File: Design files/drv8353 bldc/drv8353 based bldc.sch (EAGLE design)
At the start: 119 parts, among them IC1 DRV8353RSRGZT, J3 2X6 FEMALE, J4 B06B-HCMKK

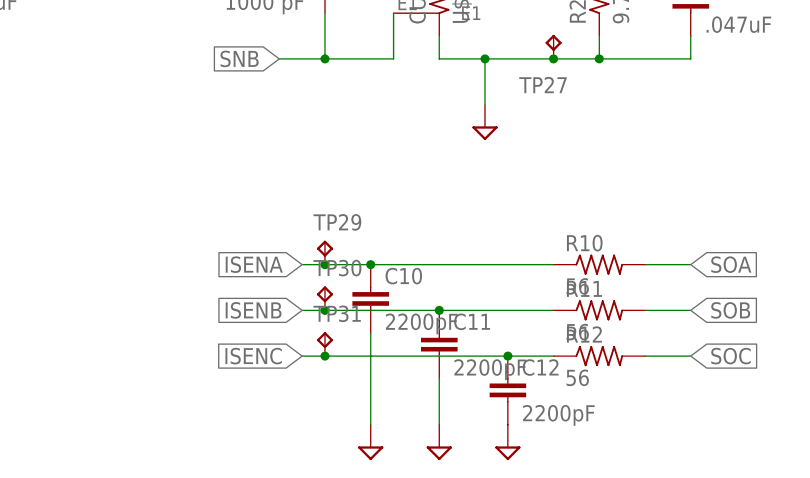
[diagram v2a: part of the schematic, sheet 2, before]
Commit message: remoeved extraneous test points
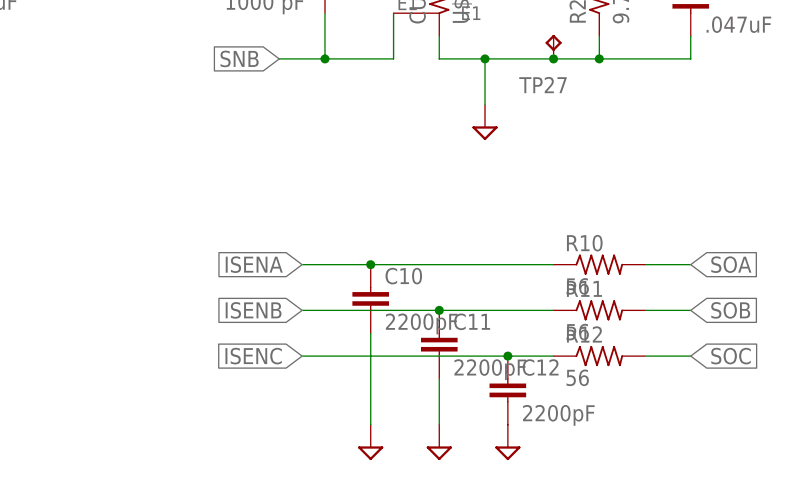
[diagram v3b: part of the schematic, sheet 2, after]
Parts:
- removed TP13, TP29, TP30, TP31, TP37, TP38, TP39: TPB1,27, testpad:TPB1,27
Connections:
- removed net N$17: TP39.TP, U$2.8
- removed net N$18: TP38.TP, U$2.6
- removed net N$19: TP37.TP, U$2.5
- net ISENA: no longer TP29.TP
- net ISENB: no longer TP30.TP
- net ISENC: no longer TP31.TP
- net VCP: no longer TP13.TP
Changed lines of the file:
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@@
 <?xml version="1.0" encoding="utf-8"?>
 <!DOCTYPE eagle SYSTEM "eagle.dtd">
-<eagle version="9.5.1">
+<eagle version="9.5.0">
 <drawing>
 <settings>
@@
 <part name="C21" library="rcl" library_urn="urn:adsk.eagle:library:334" deviceset="C-EU" device="C0805K" package3d_urn="urn:adsk.eagle:package:23681/2" value=".047 uF"/>
 <part name="C22" library="resistor" library_urn="urn:adsk.eagle:library:348" deviceset="C-EU" device="C0603K" package3d_urn="urn:adsk.eagle:package:26200/1" value="1 uF"/>
-<part name="TP13" library="testpad" library_urn="urn:adsk.eagle:library:385" deviceset="TP" device="B1,27" package3d_urn="urn:adsk.eagle:package:27944/2"/>
 <part name="C23" library="resistor" library_urn="urn:adsk.eagle:library:348" deviceset="C-EU" device="C0603K" package3d_urn="urn:adsk.eagle:package:26200/1" value=".1 uF"/>
 <part name="C25" library="rcl" library_urn="urn:adsk.eagle:library:334" deviceset="C-EU" device="C0805K" package3d_urn="urn:adsk.eagle:package:23681/2" value=".1 uF"/>
@@
 <part name="TP11" library="testpad" library_urn="urn:adsk.eagle:library:385" deviceset="TP" device="B1,27" package3d_urn="urn:adsk.eagle:package:27944/2"/>
 <part name="TP12" library="testpad" library_urn="urn:adsk.eagle:library:385" deviceset="TP" device="B1,27" package3d_urn="urn:adsk.eagle:package:27944/2"/>
-<part name="TP29" library="testpad" library_urn="urn:adsk.eagle:library:385" deviceset="TP" device="B1,27" package3d_urn="urn:adsk.eagle:package:27944/2"/>
-<part name="TP30" library="testpad" library_urn="urn:adsk.eagle:library:385" deviceset="TP" device="B1,27" package3d_urn="urn:adsk.eagle:package:27944/2"/>
-<part name="TP31" library="testpad" library_urn="urn:adsk.eagle:library:385" deviceset="TP" device="B1,27" package3d_urn="urn:adsk.eagle:package:27944/2"/>
 <part name="TP32" library="testpad" library_urn="urn:adsk.eagle:library:385" deviceset="TP" device="B1,27" package3d_urn="urn:adsk.eagle:package:27944/2"/>
 <part name="TP33" library="testpad" library_urn="urn:adsk.eagle:library:385" deviceset="TP" device="B1,27" package3d_urn="urn:adsk.eagle:package:27944/2"/>
@@
 <part name="TP35" library="testpad" library_urn="urn:adsk.eagle:library:385" deviceset="TP" device="B1,27" package3d_urn="urn:adsk.eagle:package:27944/2"/>
 <part name="TP36" library="testpad" library_urn="urn:adsk.eagle:library:385" deviceset="TP" device="B1,27" package3d_urn="urn:adsk.eagle:package:27944/2"/>
-<part name="TP37" library="testpad" library_urn="urn:adsk.eagle:library:385" deviceset="TP" device="B1,27" package3d_urn="urn:adsk.eagle:package:27944/2"/>
-<part name="TP38" library="testpad" library_urn="urn:adsk.eagle:library:385" deviceset="TP" device="B1,27" package3d_urn="urn:adsk.eagle:package:27944/2"/>
-<part name="TP39" library="testpad" library_urn="urn:adsk.eagle:library:385" deviceset="TP" device="B1,27" package3d_urn="urn:adsk.eagle:package:27944/2"/>
 <part name="U$16" library="REV BLDC" deviceset="SB50" device=""/>
 <part name="R18" library="rcl" library_urn="urn:adsk.eagle:library:334" deviceset="R-US_" device="R0603" package3d_urn="urn:adsk.eagle:package:23555/3" value="383k"/>
@@
 <attribute name="VALUE" x="-20.701" y="-54.356" size="1.778" layer="96" rot="R90"/>
 </instance>
-<instance part="TP13" gate="G$1" x="-17.78" y="-58.42" smashed="yes" rot="R180">
-<attribute name="NAME" x="-16.51" y="-59.69" size="1.778" layer="95" rot="R180"/>
-<attribute name="TP_SIGNAL_NAME" x="-19.05" y="-57.15" size="1.778" layer="97" rot="R180"/>
-</instance>
 <instance part="C23" gate="G$1" x="60.96" y="-68.58" smashed="yes">
 <attribute name="NAME" x="62.484" y="-68.199" size="1.778" layer="95"/>
@@
 <attribute name="NAME" x="-3.81" y="-62.23" size="1.778" layer="95" rot="R180"/>
 <attribute name="TP_SIGNAL_NAME" x="-3.81" y="-59.69" size="1.778" layer="97" rot="R180"/>
-</instance>
-<instance part="TP37" gate="G$1" x="-76.2" y="-127" smashed="yes" rot="R90">
-<attribute name="TP_SIGNAL_NAME" x="-74.93" y="-125.73" size="1.778" layer="97" rot="R90"/>
-</instance>
-<instance part="TP38" gate="G$1" x="-76.2" y="-129.54" smashed="yes" rot="R90">
-<attribute name="TP_SIGNAL_NAME" x="-74.93" y="-128.27" size="1.778" layer="97" rot="R90"/>
-</instance>
-<instance part="TP39" gate="G$1" x="-76.2" y="-134.62" smashed="yes" rot="R90">
-<attribute name="TP_SIGNAL_NAME" x="-74.93" y="-133.35" size="1.778" layer="97" rot="R90"/>
 </instance>
 <instance part="BB2" gate="1" x="119.38" y="-104.14" smashed="yes">
@@
 <segment>
 <pinref part="IC1" gate="G$1" pin="VCP"/>
-<wire x1="-2.54" y1="-55.88" x2="-17.78" y2="-55.88" width="0.1524" layer="91"/>
+<wire x1="-2.54" y1="-55.88" x2="-20.32" y2="-55.88" width="0.1524" layer="91"/>
 <pinref part="C22" gate="G$1" pin="2"/>
-<pinref part="TP13" gate="G$1" pin="TP"/>
-<wire x1="-17.78" y1="-55.88" x2="-20.32" y2="-55.88" width="0.1524" layer="91"/>
-<junction x="-17.78" y="-55.88"/>
 </segment>
 </net>
@@
 <pinref part="R4" gate="G$1" pin="1"/>
 <wire x1="-68.58" y1="-83.82" x2="-55.88" y2="-83.82" width="0.1524" layer="91"/>
-</segment>
-</net>
-<net name="N$17" class="0">
-<segment>
-<wire x1="-68.58" y1="-134.62" x2="-73.66" y2="-134.62" width="0.1524" layer="91"/>
-<pinref part="TP39" gate="G$1" pin="TP"/>
-<pinref part="U$2" gate="G$1" pin="8"/>
-</segment>
-</net>
-<net name="N$18" class="0">
-<segment>
-<wire x1="-68.58" y1="-129.54" x2="-73.66" y2="-129.54" width="0.1524" layer="91"/>
-<pinref part="TP38" gate="G$1" pin="TP"/>
-<pinref part="U$2" gate="G$1" pin="6"/>
-</segment>
-</net>
-<net name="N$19" class="0">
-<segment>
-<wire x1="-68.58" y1="-127" x2="-73.66" y2="-127" width="0.1524" layer="91"/>
-<pinref part="TP37" gate="G$1" pin="TP"/>
-<pinref part="U$2" gate="G$1" pin="5"/>
 </segment>
 </net>
@@
 <attribute name="NAME" x="114.935" y="58.674" size="1.778" layer="95" rot="R90"/>
 <attribute name="VALUE" x="120.269" y="58.674" size="1.778" layer="96" rot="R90"/>
-</instance>
-<instance part="TP29" gate="G$1" x="15.24" y="-15.24" smashed="yes">
-<attribute name="NAME" x="13.97" y="-13.97" size="1.778" layer="95"/>
-<attribute name="TP_SIGNAL_NAME" x="16.51" y="-16.51" size="1.778" layer="97"/>
-</instance>
-<instance part="TP30" gate="G$1" x="15.24" y="-20.32" smashed="yes">
-<attribute name="NAME" x="13.97" y="-19.05" size="1.778" layer="95"/>
-<attribute name="TP_SIGNAL_NAME" x="16.51" y="-21.59" size="1.778" layer="97"/>
-</instance>
-<instance part="TP31" gate="G$1" x="15.24" y="-25.4" smashed="yes">
-<attribute name="NAME" x="13.97" y="-24.13" size="1.778" layer="95"/>
-<attribute name="TP_SIGNAL_NAME" x="16.51" y="-26.67" size="1.778" layer="97"/>
 </instance>
 <instance part="U$3" gate="G$1" x="-55.88" y="12.7" smashed="yes" rot="MR90">
@@
 <wire x1="40.64" y1="-17.78" x2="20.32" y2="-17.78" width="0.1524" layer="91"/>
 <pinref part="C10" gate="G$1" pin="1"/>
-<wire x1="20.32" y1="-17.78" x2="15.24" y2="-17.78" width="0.1524" layer="91"/>
+<wire x1="20.32" y1="-17.78" x2="12.7" y2="-17.78" width="0.1524" layer="91"/>
 <junction x="20.32" y="-17.78"/>
 <label x="12.7" y="-17.78" size="1.778" layer="95" rot="R180" xref="yes"/>
-<pinref part="TP29" gate="G$1" pin="TP"/>
-<wire x1="15.24" y1="-17.78" x2="12.7" y2="-17.78" width="0.1524" layer="91"/>
-<junction x="15.24" y="-17.78"/>
 </segment>
 </net>
@@
 <wire x1="40.64" y1="-22.86" x2="27.94" y2="-22.86" width="0.1524" layer="91"/>
 <pinref part="C11" gate="G$1" pin="1"/>
-<wire x1="27.94" y1="-22.86" x2="15.24" y2="-22.86" width="0.1524" layer="91"/>
+<wire x1="27.94" y1="-22.86" x2="12.7" y2="-22.86" width="0.1524" layer="91"/>
 <junction x="27.94" y="-22.86"/>
 <label x="12.7" y="-22.86" size="1.778" layer="95" rot="R180" xref="yes"/>
-<pinref part="TP30" gate="G$1" pin="TP"/>
-<wire x1="15.24" y1="-22.86" x2="12.7" y2="-22.86" width="0.1524" layer="91"/>
-<junction x="15.24" y="-22.86"/>
 </segment>
 </net>
@@
 <wire x1="40.64" y1="-27.94" x2="35.56" y2="-27.94" width="0.1524" layer="91"/>
 <pinref part="C12" gate="G$1" pin="1"/>
-<wire x1="35.56" y1="-27.94" x2="15.24" y2="-27.94" width="0.1524" layer="91"/>
+<wire x1="35.56" y1="-27.94" x2="12.7" y2="-27.94" width="0.1524" layer="91"/>
 <junction x="35.56" y="-27.94"/>
 <label x="12.7" y="-27.94" size="1.778" layer="95" rot="R180" xref="yes"/>
-<pinref part="TP31" gate="G$1" pin="TP"/>
-<wire x1="15.24" y1="-27.94" x2="12.7" y2="-27.94" width="0.1524" layer="91"/>
-<junction x="15.24" y="-27.94"/>
-</segment>
-</net>
+</segment>
+</net>

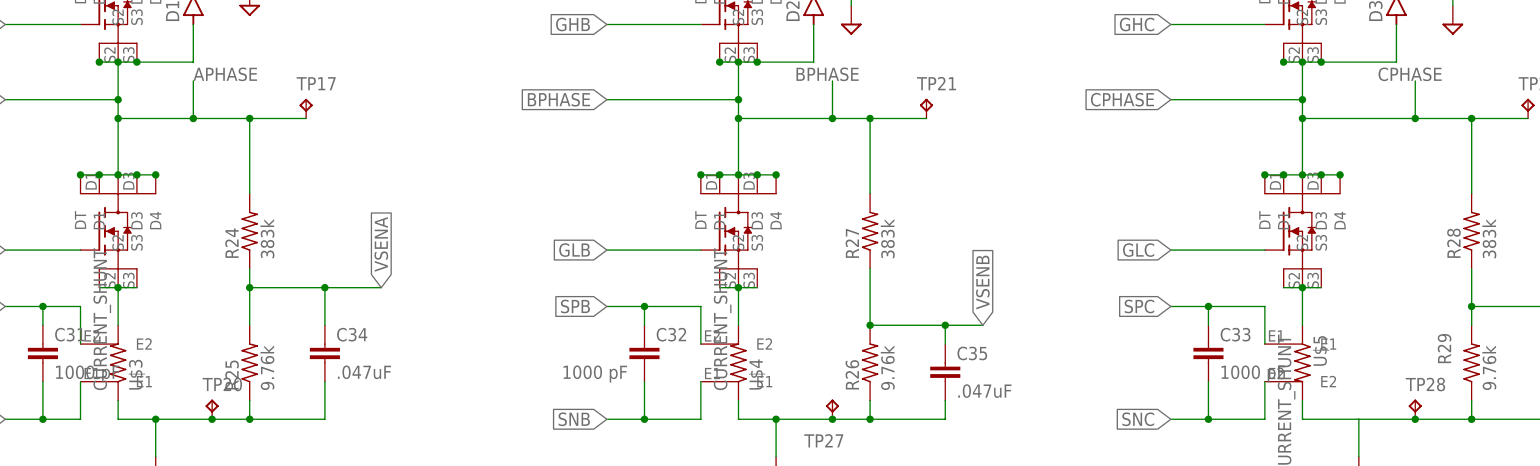
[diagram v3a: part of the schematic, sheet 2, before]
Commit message: added low side flybacks
added low side flybacks
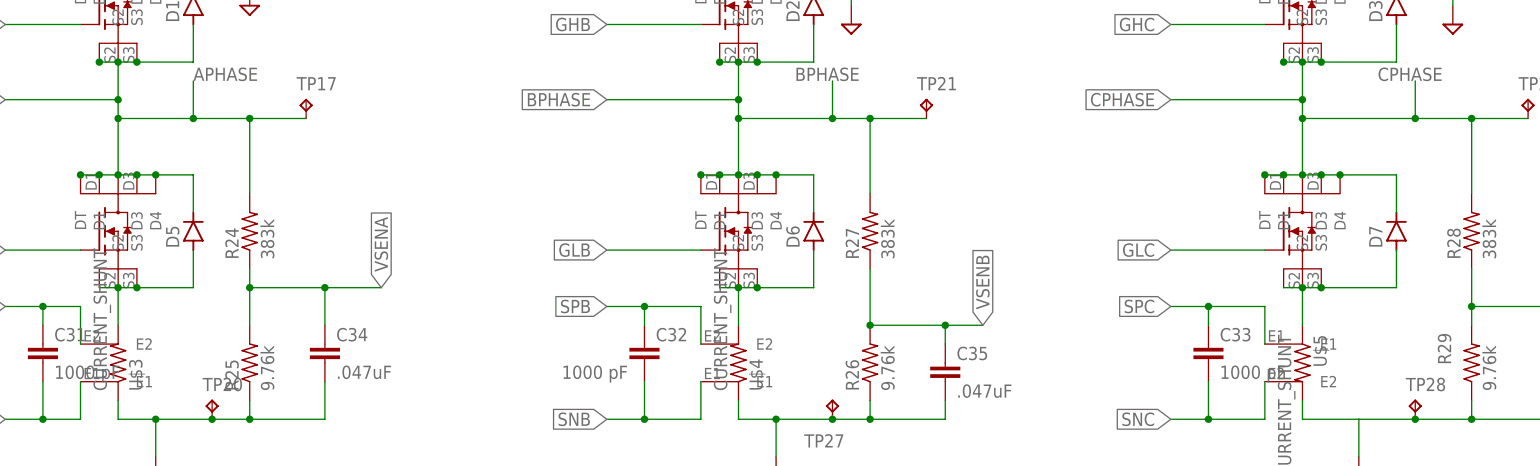
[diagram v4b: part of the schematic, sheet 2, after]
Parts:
- added D5, D6, D7: (no value), REV BLDC:D-SOD123
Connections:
- net APHASE: now also D5.C
- net BPHASE: now also D6.C
- net CPHASE: now also D7.C
- net N$22: now also D6.A
- net N$24: now also D5.A
- net N$27: now also D7.A
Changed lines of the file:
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@@
 <part name="R5" library="resistor" library_urn="urn:adsk.eagle:library:348" deviceset="R-US_" device="R0603" package3d_urn="urn:adsk.eagle:package:26057/1" value="0"/>
 <part name="TP19" library="testpad" library_urn="urn:adsk.eagle:library:385" deviceset="TP" device="B1,27" package3d_urn="urn:adsk.eagle:package:27944/2"/>
+<part name="D5" library="REV BLDC" deviceset="D-" device="SOD123" package3d_urn="urn:adsk.eagle:package:26308/2"/>
+<part name="D6" library="REV BLDC" deviceset="D-" device="SOD123" package3d_urn="urn:adsk.eagle:package:26308/2"/>
+<part name="D7" library="REV BLDC" deviceset="D-" device="SOD123" package3d_urn="urn:adsk.eagle:package:26308/2"/>
 </parts>
 <sheets>
@@
 <attribute name="NAME" x="125.984" y="71.501" size="1.778" layer="95"/>
 <attribute name="VALUE" x="125.984" y="66.421" size="1.778" layer="96"/>
+</instance>
+<instance part="D5" gate="G$1" x="-45.72" y="30.48" smashed="yes" rot="R90">
+<attribute name="NAME" x="-47.625" y="28.194" size="1.778" layer="95" rot="R90"/>
+<attribute name="VALUE" x="-41.021" y="27.686" size="1.778" layer="96" rot="R90"/>
+</instance>
+<instance part="D6" gate="G$1" x="38.1" y="30.48" smashed="yes" rot="R90">
+<attribute name="NAME" x="36.195" y="28.194" size="1.778" layer="95" rot="R90"/>
+<attribute name="VALUE" x="42.799" y="27.686" size="1.778" layer="96" rot="R90"/>
+</instance>
+<instance part="D7" gate="G$1" x="116.84" y="30.48" smashed="yes" rot="R90">
+<attribute name="NAME" x="114.935" y="28.194" size="1.778" layer="95" rot="R90"/>
+<attribute name="VALUE" x="121.539" y="27.686" size="1.778" layer="96" rot="R90"/>
 </instance>
 </instances>
@@
 <pinref part="U$3" gate="G$1" pin="I2"/>
 <wire x1="-55.88" y1="17.78" x2="-55.88" y2="22.86" width="0.1524" layer="91"/>
+<pinref part="D5" gate="G$1" pin="A"/>
+<wire x1="-45.72" y1="27.94" x2="-45.72" y2="22.86" width="0.1524" layer="91"/>
+<wire x1="-45.72" y1="22.86" x2="-53.34" y2="22.86" width="0.1524" layer="91"/>
+<junction x="-53.34" y="22.86"/>
 </segment>
 </net>
@@
 <pinref part="U$4" gate="G$1" pin="I2"/>
 <wire x1="27.94" y1="17.78" x2="27.94" y2="22.86" width="0.1524" layer="91"/>
+<pinref part="D6" gate="G$1" pin="A"/>
+<wire x1="38.1" y1="27.94" x2="38.1" y2="22.86" width="0.1524" layer="91"/>
+<wire x1="38.1" y1="22.86" x2="30.48" y2="22.86" width="0.1524" layer="91"/>
+<junction x="30.48" y="22.86"/>
 </segment>
 </net>
@@
 <pinref part="U$5" gate="G$1" pin="I1"/>
 <wire x1="104.14" y1="22.86" x2="104.14" y2="17.78" width="0.1524" layer="91"/>
+<pinref part="D7" gate="G$1" pin="A"/>
+<wire x1="116.84" y1="27.94" x2="116.84" y2="22.86" width="0.1524" layer="91"/>
+<wire x1="116.84" y1="22.86" x2="106.68" y2="22.86" width="0.1524" layer="91"/>
+<junction x="106.68" y="22.86"/>
 </segment>
 </net>
@@
 <wire x1="-45.72" y1="53.34" x2="-45.72" y2="58.42" width="0.1524" layer="91"/>
 <wire x1="-71.12" y1="48.26" x2="-55.88" y2="48.26" width="0.1524" layer="91"/>
+<pinref part="D5" gate="G$1" pin="C"/>
+<wire x1="-45.72" y1="33.02" x2="-45.72" y2="38.1" width="0.1524" layer="91"/>
+<wire x1="-45.72" y1="38.1" x2="-50.8" y2="38.1" width="0.1524" layer="91"/>
 </segment>
 </net>
@@
 <pinref part="D2" gate="G$1" pin="A"/>
 <wire x1="38.1" y1="53.34" x2="38.1" y2="58.42" width="0.1524" layer="91"/>
+<pinref part="D6" gate="G$1" pin="C"/>
+<wire x1="38.1" y1="33.02" x2="38.1" y2="38.1" width="0.1524" layer="91"/>
+<wire x1="38.1" y1="38.1" x2="33.02" y2="38.1" width="0.1524" layer="91"/>
 </segment>
 </net>
@@
 <wire x1="106.68" y1="53.34" x2="116.84" y2="53.34" width="0.1524" layer="91"/>
 <wire x1="116.84" y1="53.34" x2="116.84" y2="58.42" width="0.1524" layer="91"/>
-</segment>
-</net>
+<pinref part="D7" gate="G$1" pin="C"/>
+<wire x1="116.84" y1="33.02" x2="116.84" y2="38.1" width="0.1524" layer="91"/>
+<wire x1="116.84" y1="38.1" x2="109.22" y2="38.1" width="0.1524" layer="91"/>
+</segment>
+</net>
